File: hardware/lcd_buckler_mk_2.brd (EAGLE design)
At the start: 52 x 50 mm, 16 parts, among them IC1 ATTINY84

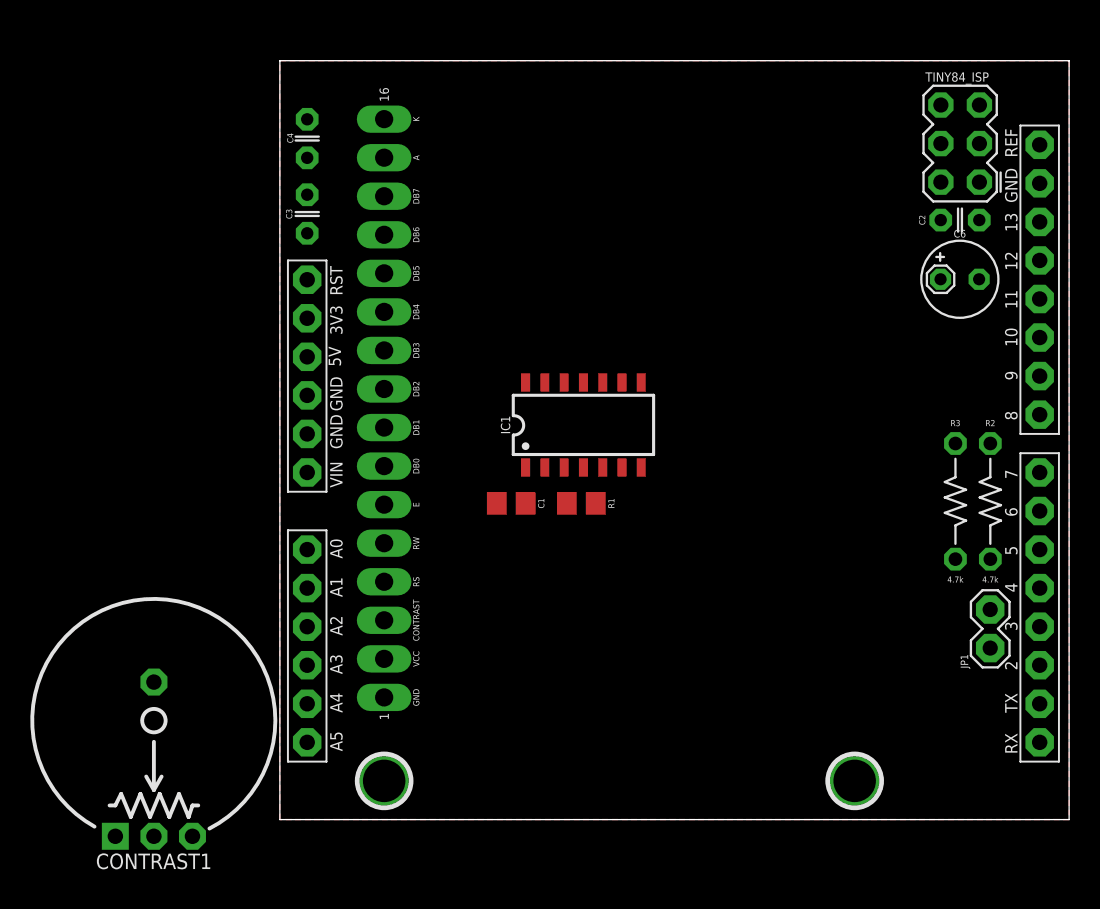
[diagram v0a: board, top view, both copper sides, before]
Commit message: version 2 ready for fab. added lcd connections and trimpots to both sides in case i need to reverse/flip something. disconnect for i2c pull-ups as i'm wondering if those are causing problems.
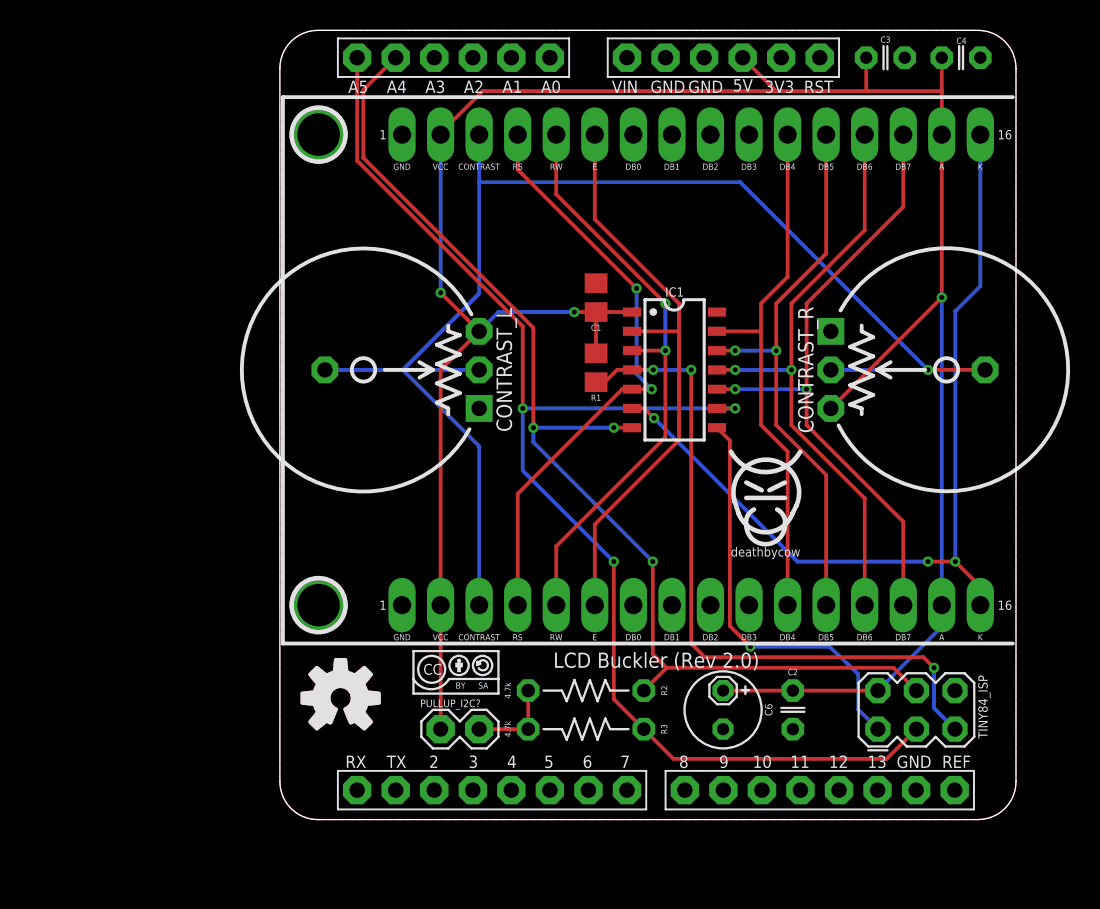
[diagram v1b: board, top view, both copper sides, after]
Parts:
- removed CONTRAST1: 10k, A_butts:POT-THUMBWHEEL
- removed JP1: M02PTH, A_butts:1X02
- removed LCD: LCD-16x2, A_butts:LCD-16X2-PINS-ONLY
- added CONTRAST_L, CONTRAST_R: 10k, A_butts:POT-THUMBWHEEL
- added LCD_BOTTOM, LCD_TOP: LCD-16x2, A_butts:LCD-16X2-PINS-ONLY
- added PULLUP_I2C?: M02PTH, A_butts:1X02
- added U$1: (no value), A_butts:COW
- added U$2: (no value), A_butts:COW_SMALL
- added U$3, U$4: (no value), A_butts:CC-BY-SA-4.0-NO-URL
- added U$5: (no value), A_butts:OSHWLOGO_TOP_0.2_A
- added U$6: (no value), A_butts:OSHWLOGO_BOT_0.2_A
- moved SHIELD 45.1 mm to (5.09, 1.94), turned to 90 degrees
- moved C4 43.4 mm to (44.9, 50.2), turned to 0 degrees
- moved H1 42.8 mm to (2.55, 45.1), turned to 270 degrees
- moved C3 39.5 mm to (39.9, 50.2), turned to 0 degrees
- moved TINY84_ISP 37.4 mm to (41.9, 7.23), turned to 0 degrees
- moved H2 37.2 mm to (2.55, 14.1), turned to 270 degrees
- moved C2 34.1 mm to (33.8, 7.23), turned to 270 degrees
- moved C6 32.4 mm to (29.2, 7.23), turned to 270 degrees
- moved R2 29.4 mm to (20.2, 8.50), turned to 180 degrees
- moved R3 28.6 mm to (20.2, 5.96), turned to 180 degrees
- moved C1 14.7 mm to (20.8, 34.4), turned to 90 degrees
- moved R1 8.99 mm to (20.8, 29.8), turned to 90 degrees
- moved IC1 7.01 mm to (26.0, 29.6), turned to 270 degrees
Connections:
- net 5V: now also CONTRAST_L.3, CONTRAST_R.3, LCD_BOTTOM.15, LCD_BOTTOM.2, LCD_TOP.15, LCD_TOP.2, PULLUP_I2C?.1; no longer CONTRAST1.3, JP1.1, LCD.15, LCD.2
- net BACKLIGHT: now also LCD_BOTTOM.16, LCD_TOP.16; no longer LCD.16
- net CON: now also CONTRAST_L.2, CONTRAST_L.2@1, CONTRAST_R.2, CONTRAST_R.2@1, LCD_BOTTOM.3, LCD_TOP.3; no longer CONTRAST1.2, CONTRAST1.2@1, LCD.3
- net DB4: now also LCD_BOTTOM.11, LCD_TOP.11; no longer LCD.11
- net DB5: now also LCD_BOTTOM.12, LCD_TOP.12; no longer LCD.12
- net DB6: now also LCD_BOTTOM.13, LCD_TOP.13; no longer LCD.13
- net DB7: now also LCD_BOTTOM.14, LCD_TOP.14; no longer LCD.14
- net E: now also LCD_BOTTOM.6, LCD_TOP.6; no longer LCD.6
- net GND: now also CONTRAST_L.1, CONTRAST_R.1, LCD_BOTTOM.1, LCD_TOP.1; no longer CONTRAST1.1, LCD.1
- net N$1: now also PULLUP_I2C?.2; no longer JP1.2
- net RS: now also LCD_BOTTOM.4, LCD_TOP.4; no longer LCD.4
- net RW: now also LCD_BOTTOM.5, LCD_TOP.5; no longer LCD.5
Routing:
- net 5V: track 0.00 -> 158.1 mm, vias 0 -> 3
- net CON: track 0.00 -> 90.2 mm, vias 0 -> 1
- net SCK/SCL: track 0.00 -> 86.8 mm, vias 0 -> 3
- net MOSISDA: track 0.00 -> 75.1 mm, vias 0 -> 3
- net BACKLIGHT: track 0.00 -> 57.8 mm, vias 0 -> 3
- net RESET: track 0.00 -> 45.9 mm, vias 0 -> 3
- net DB7: track 0.00 -> 42.2 mm, vias 0 -> 2
- net DB6: track 0.00 -> 39.9 mm, vias 0 -> 2
- net RS: track 0.00 -> 39.5 mm, vias 0 -> 2
- net RW: track 0.00 -> 39.2 mm, vias 0 -> 2
- net E: track 0.00 -> 38.7 mm
- net DB5: track 0.00 -> 37.6 mm, vias 0 -> 2
- net DB4: track 0.00 -> 35.3 mm
- net MISO: track 0.00 -> 27.3 mm, vias 0 -> 1
- net N$1: track 0.00 -> 5.77 mm
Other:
- board size 52 x 50 mm -> 48.5 x 52 mm
- board text added: "LCD Buckler"
- board text added: "LCD Buckler (Rev 2.0)"
- board text added: "by schizobovine <sean@yak.net> Rev 2.0"
